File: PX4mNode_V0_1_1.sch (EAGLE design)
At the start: 140 parts, among them J201 DF13C-6P-1.25V, J202 DF13C-6P-1.25V, J203 DF13C-6P-1.25V, J301 DF13C-4P-1.25V, J401 DF13C-7P-1.25V, J402 DF13-4P-1.25V, J403 DF13C-4P-1.25V, J404 DF13C-4P-1.25V, J405 DF13C-4P-1.25V, J801 DF13C-3P-1.25V, M3_MOUNT1101 MOUNT-HOLE3.1MM, M3_MOUNT1102 MOUNT-HOLE3.1MM, M3_MOUNT1103 MOUNT-HOLE3.1MM, M3_MOUNT1104 MOUNT-HOLE3.1MM, U101 STM32F4X7VX, U401 MAX3051, U402 MAX3051, X101 3.2x2.5 mm / 24 MHz / 15 ppm

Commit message: Renumber
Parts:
- renumbered JP1 to JP1001, JP2 to JP1002, JP3 to JP702, R1 to R1001, R2 to R1002
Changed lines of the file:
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@@
 <attribute name="PARTNO" value="MSS1P4-M3/89A"/>
 </part>
-<part name="JP1" library="SparkFun-Connectors" deviceset="M01" device="SMD-4.5X1.5"/>
-<part name="JP2" library="SparkFun-Connectors" deviceset="M01" device="SMD-4.5X1.5"/>
-<part name="R1" library="pixhawk2" deviceset="RESISTOR" device="0402-RES" value="220R">
+<part name="JP1001" library="SparkFun-Connectors" deviceset="M01" device="SMD-4.5X1.5"/>
+<part name="JP1002" library="SparkFun-Connectors" deviceset="M01" device="SMD-4.5X1.5"/>
+<part name="R1001" library="pixhawk2" deviceset="RESISTOR" device="0402-RES" value="220R">
 <attribute name="PARTNO" value="RC0402FR-07220RL"/>
 </part>
-<part name="R2" library="pixhawk2" deviceset="RESISTOR" device="0402-RES" value="220R">
+<part name="R1002" library="pixhawk2" deviceset="RESISTOR" device="0402-RES" value="220R">
 <attribute name="PARTNO" value="RC0402FR-07220RL"/>
 </part>
-<part name="JP3" library="SparkFun-Connectors" deviceset="M01" device="SMD-4.5X1.5"/>
+<part name="JP702" library="SparkFun-Connectors" deviceset="M01" device="SMD-4.5X1.5"/>
 </parts>
 <sheets>
@@
 <attribute name="PARTNO" x="205.74" y="127" size="1.778" layer="96" rot="MR90" display="off"/>
 </instance>
-<instance part="JP3" gate="G$1" x="195.58" y="91.44"/>
+<instance part="JP702" gate="G$1" x="195.58" y="91.44"/>
 </instances>
 <busses>
@@
 <wire x1="233.68" y1="91.44" x2="233.68" y2="96.52" width="0.1524" layer="91"/>
 <junction x="223.52" y="91.44"/>
-<pinref part="JP3" gate="G$1" pin="1"/>
+<pinref part="JP702" gate="G$1" pin="1"/>
 <wire x1="203.2" y1="91.44" x2="223.52" y2="91.44" width="0.1524" layer="91"/>
 </segment>
@@
 <instance part="J1001" gate="-CH7" x="101.6" y="129.54"/>
 <instance part="J1001" gate="-CH8" x="101.6" y="134.62"/>
-<instance part="JP1" gate="G$1" x="106.68" y="71.12" rot="R180"/>
-<instance part="JP2" gate="G$1" x="106.68" y="53.34" rot="R180"/>
-<instance part="R1" gate="G$1" x="71.12" y="71.12" rot="R180">
+<instance part="JP1001" gate="G$1" x="106.68" y="71.12" rot="R180"/>
+<instance part="JP1002" gate="G$1" x="106.68" y="53.34" rot="R180"/>
+<instance part="R1001" gate="G$1" x="71.12" y="71.12" rot="R180">
 <attribute name="PARTNO" x="71.12" y="71.12" size="1.778" layer="96" rot="R90" display="off"/>
 </instance>
-<instance part="R2" gate="G$1" x="71.12" y="53.34" rot="R180">
+<instance part="R1002" gate="G$1" x="71.12" y="53.34" rot="R180">
 <attribute name="PARTNO" x="71.12" y="53.34" size="1.778" layer="96" rot="R90" display="off"/>
 </instance>
@@
 <net name="N$19" class="0">
 <segment>
-<pinref part="JP1" gate="G$1" pin="1"/>
-<pinref part="R1" gate="G$1" pin="1"/>
+<pinref part="JP1001" gate="G$1" pin="1"/>
+<pinref part="R1001" gate="G$1" pin="1"/>
 <wire x1="99.06" y1="71.12" x2="76.2" y2="71.12" width="0.1524" layer="91"/>
 </segment>
@@
 <net name="N$23" class="0">
 <segment>
-<pinref part="JP2" gate="G$1" pin="1"/>
-<pinref part="R2" gate="G$1" pin="1"/>
+<pinref part="JP1002" gate="G$1" pin="1"/>
+<pinref part="R1002" gate="G$1" pin="1"/>
 <wire x1="99.06" y1="53.34" x2="76.2" y2="53.34" width="0.1524" layer="91"/>
 </segment>
@@
 <wire x1="40.64" y1="71.12" x2="66.04" y2="71.12" width="0.1524" layer="91"/>
 <label x="40.64" y="71.12" size="1.27" layer="95" rot="R180" xref="yes"/>
-<pinref part="R1" gate="G$1" pin="2"/>
+<pinref part="R1001" gate="G$1" pin="2"/>
 </segment>
 </net>
@@
 <label x="40.64" y="53.34" size="1.27" layer="95" rot="R180" xref="yes"/>
 <wire x1="40.64" y1="53.34" x2="66.04" y2="53.34" width="0.1524" layer="91"/>
-<pinref part="R2" gate="G$1" pin="2"/>
+<pinref part="R1002" gate="G$1" pin="2"/>
 </segment>
 </net>

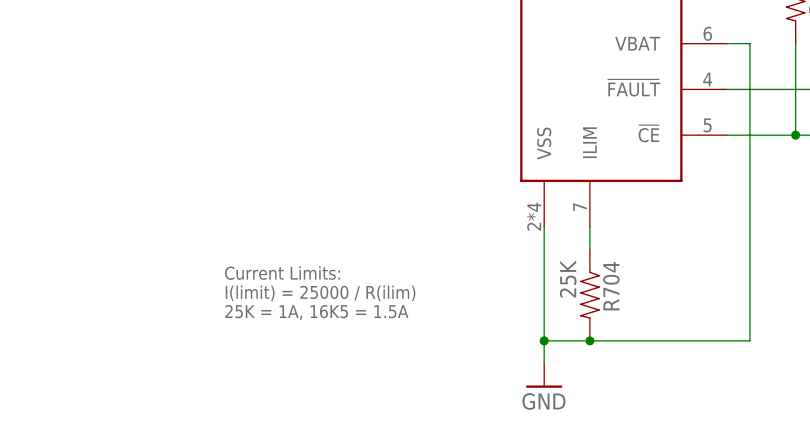
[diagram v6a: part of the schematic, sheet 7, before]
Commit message: BOM EXLUDES added to solder jumpers, 0.1" conns etc..
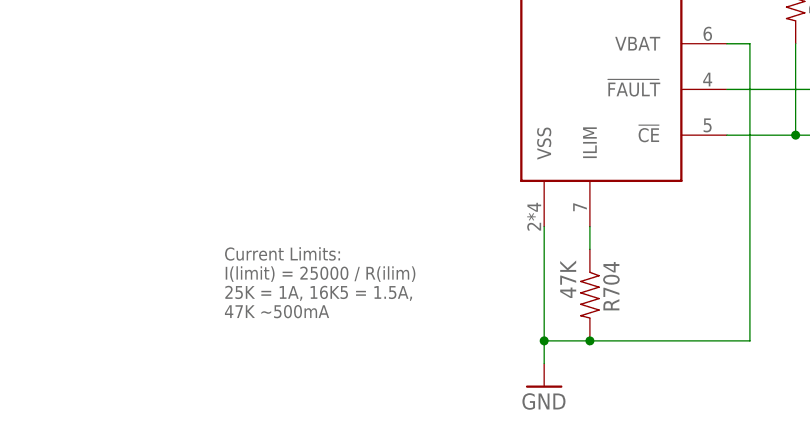
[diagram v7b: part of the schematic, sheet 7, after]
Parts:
- D901, J$401, J1001, JP1001, JP1002, JP201, JP202, JP701, JP702, JP901, SJ401, SJ402, SJ403: BOM (none) -> EXCLUDE
- R704: value 25K -> 47K; PARTNO RMCF0402FT25K5 -> RMCF0402FT47K
- U$202: PARTNO (none) -> 74LVC2GU04
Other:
- note added: "Current Limits: I(limit) = 25000 / R(ilim) 25K = 1A, 16K5 = 1.5A, 47K ~500mA"
- note added: "DO NOT FIT"
- note removed: "Current Limits: I(limit) = 25000 / R(ilim) 25K = 1A, 16K5 = 1.5A"

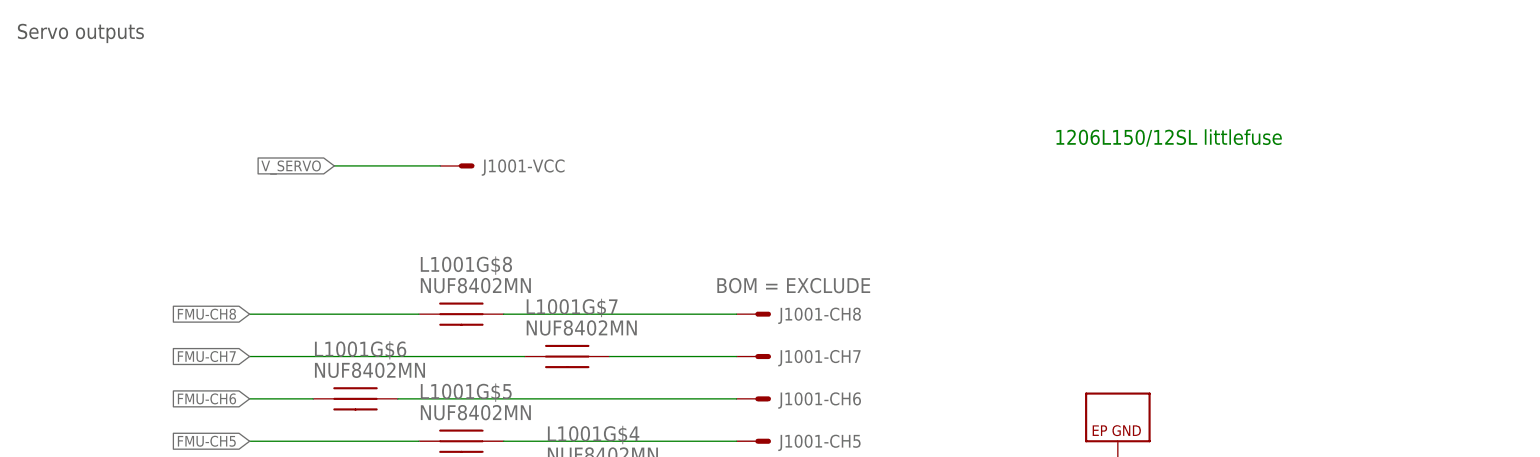
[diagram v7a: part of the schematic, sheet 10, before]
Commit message: a few bom tweaks
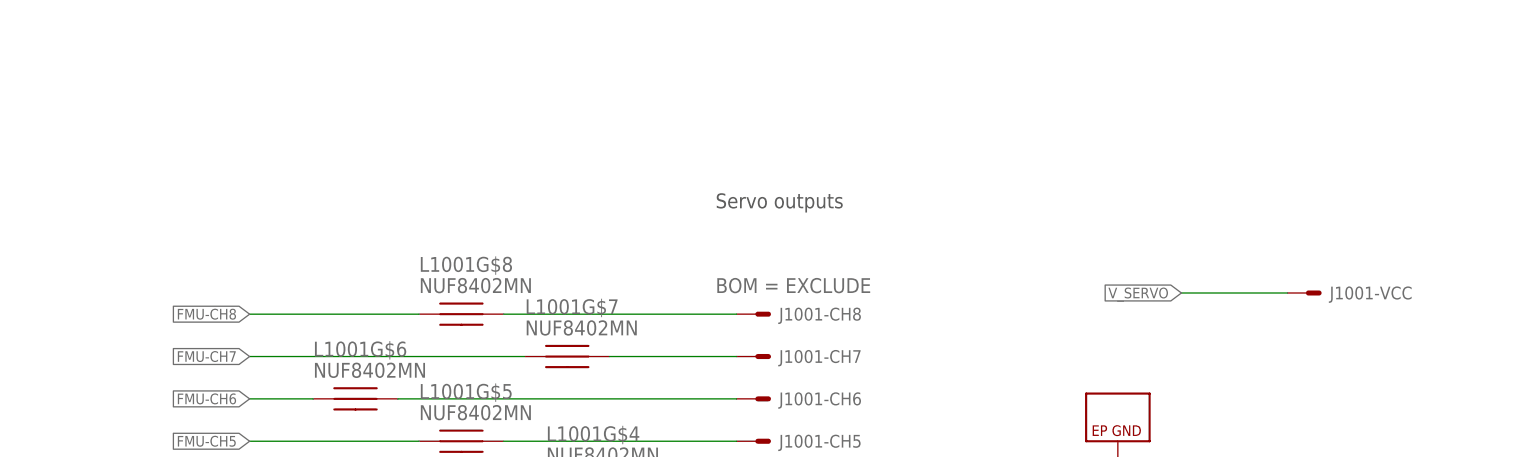
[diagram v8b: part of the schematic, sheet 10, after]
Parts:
- D902, D903: PARTNO (none) -> B340A
- J301, J403, J404, J405: device con-hirose-df13:DF13-4P-1.25V -> PX4FMUlite_V0_1:DF13-4P-1.25V
- J402: value DF13-4P-1.25V -> DF13C-4P-1.25V; device con-hirose-df13:DF13-4P-1.25V -> PX4FMUlite_V0_1:DF13-4P-1.25V
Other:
- note added: "FMU Power FMU Reset Battery backup Peripheral power control"
- note added: "FMU Serial ports SBUS interface Spektrum interface"
- note added: "FMU SoC Ports"
- note added: "LEDs Safety switch"
- note added: "Power regulation"
- note added: "SPI Dual I2C Dual CAN Aux ADC ports"
- note added: "USB Flash SWD Debug connector"
- note removed: "1206L150/12SL littlefuse"
- note removed: "FMU Power and Reset"
- note removed: "FMU Serial ports"
- note removed: "FMU SoC Ports FRAM"
- note removed: "LEDs Piezo driver Safety switch"
- note removed: "Power source selector"
- note removed: "SPI I2C Analog pressure CAN Aux ADC ports"
- note removed: "USB Flash Expansion"
- moved on the sheet: J1001-VCC
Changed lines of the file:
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@@
 <attribute name="PARTNO" value="*"/>
 </part>
-<part name="J301" library="con-hirose-df13" deviceset="DF13-4P-1.25" device="V" value="DF13C-4P-1.25V">
+<part name="J301" library="PX4FMUlite_V0_1" deviceset="DF13-4P-1.25" device="V" value="DF13C-4P-1.25V">
 <attribute name="PARTNO" value="DF13C-4P-1.25V(20)"/>
 </part>
@@
 </part>
 <part name="GND31" library="pixhawk2" deviceset="GND" device=""/>
-<part name="J403" library="con-hirose-df13" deviceset="DF13-4P-1.25" device="V" value="DF13C-4P-1.25V">
+<part name="J403" library="PX4FMUlite_V0_1" deviceset="DF13-4P-1.25" device="V" value="DF13C-4P-1.25V">
 <attribute name="PARTNO" value="DF13C-4P-1.25V(20)"/>
 </part>
@@
 <attribute name="PARTNO" value="MAX3051EKA"/>
 </part>
-<part name="J405" library="con-hirose-df13" deviceset="DF13-4P-1.25" device="V" value="DF13C-4P-1.25V">
+<part name="J405" library="PX4FMUlite_V0_1" deviceset="DF13-4P-1.25" device="V" value="DF13C-4P-1.25V">
 <attribute name="PARTNO" value="DF13C-4P-1.25V(20)"/>
 </part>
@@
 </part>
 <part name="GND15" library="pixhawk2" deviceset="GND" device=""/>
-<part name="J402" library="con-hirose-df13" deviceset="DF13-4P-1.25" device="V" value="DF13-4P-1.25V">
+<part name="J402" library="PX4FMUlite_V0_1" deviceset="DF13-4P-1.25" device="V" value="DF13C-4P-1.25V">
 <attribute name="PARTNO" value="DF13C-4P-1.25V(20)"/>
 </part>
@@
 <attribute name="PARTNO" value="MAX3051EKA"/>
 </part>
-<part name="J404" library="con-hirose-df13" deviceset="DF13-4P-1.25" device="V" value="DF13C-4P-1.25V">
+<part name="J404" library="PX4FMUlite_V0_1" deviceset="DF13-4P-1.25" device="V" value="DF13C-4P-1.25V">
 <attribute name="PARTNO" value="DF13C-4P-1.25V(20)"/>
 </part>
@@
 <attribute name="BOM" value="EXCLUDE"/>
 </part>
-<part name="D902" library="SparkFun-DiscreteSemi" deviceset="DIODE" device="SMA" value="B340A"/>
-<part name="D903" library="SparkFun-DiscreteSemi" deviceset="DIODE" device="SMA" value="B340A"/>
+<part name="D902" library="SparkFun-DiscreteSemi" deviceset="DIODE" device="SMA" value="B340A">
+<attribute name="PARTNO" value="B340A"/>
+</part>
+<part name="D903" library="SparkFun-DiscreteSemi" deviceset="DIODE" device="SMA" value="B340A">
+<attribute name="PARTNO" value="B340A"/>
+</part>
 <part name="U$601" library="PX4lite" deviceset="TPS6303X" device=""/>
 <part name="L$601" library="ti_tps_soln2" deviceset="XFL4020-222MEB" device=""/>
@@
 <plain>
 <text x="162.56" y="15.24" size="2.1844" layer="94" font="vector" ratio="10">FMU SoC Ports
-FRAM</text>
+</text>
 <text x="7.62" y="5.08" size="1.27" layer="91">Note: MAG/ACCEL/GYRO_DRDY pins chosen
 for both timer capture and separate
@@
 <sheet>
 <plain>
-<text x="165.1" y="17.78" size="2.1844" layer="94">FMU Serial ports</text>
+<text x="165.1" y="17.78" size="2.1844" layer="94">FMU Serial ports
+SBUS interface
+Spektrum interface</text>
 <text x="233.68" y="121.92" size="1.778" layer="97">SERIAL2</text>
 <text x="233.68" y="154.94" size="1.778" layer="97">SERIAL1</text>
@@
 <text x="162.56" y="12.7" size="2.1844" layer="94">USB
 Flash
-Expansion</text>
+SWD Debug connector</text>
 <text x="93.98" y="111.76" size="1.4224" layer="97">To be used with panel-
 mount micro USB connectors:
@@
 <text x="228.6" y="170.18" size="1.778" layer="97">AUX ADC PORTS</text>
 <text x="165.1" y="7.62" size="1.778" layer="94">SPI
-I2C
-Analog pressure
-CAN
+Dual I2C
+Dual CAN
 Aux ADC ports</text>
 <text x="22.86" y="170.18" size="1.778" layer="91">Note: SPI port is UNBUFFERED; only suitable for short connections.</text>
@@
 <sheet>
 <plain>
-<text x="165.1" y="17.78" size="2.1844" layer="94">Power source selector</text>
+<text x="165.1" y="17.78" size="2.1844" layer="94">Power regulation</text>
 </plain>
 <instances>
@@
 <sheet>
 <plain>
-<text x="165.1" y="17.78" size="1.9304" layer="94" font="vector" ratio="10">FMU Power and Reset</text>
+<text x="165.1" y="7.62" size="1.9304" layer="94" font="vector" ratio="10">FMU Power
+FMU Reset
+Battery backup
+Peripheral power control</text>
 <text x="187.96" y="170.18" size="1.27" layer="97" font="vector">Bypass caps as close to device pins as possible.</text>
 <text x="71.12" y="160.02" size="1.27" layer="97">Note: Maximise copper area connected
@@
 <plain>
 <text x="165.1" y="10.16" size="2.1844" layer="94">LEDs
-Piezo driver
 Safety switch</text>
 <text x="78.74" y="78.74" size="1.778" layer="97">Switch: E-Switch LP1OA1AR</text>
@@
 <attribute name="BOM" x="81.28" y="86.36" size="1.778" layer="96" rot="R90" display="off"/>
 </instance>
-<instance part="D902" gate="G$1" x="104.14" y="127"/>
-<instance part="D903" gate="G$1" x="116.84" y="139.7" rot="R270"/>
+<instance part="D902" gate="G$1" x="104.14" y="127">
+<attribute name="PARTNO" x="104.14" y="127" size="1.778" layer="96" display="off"/>
+</instance>
+<instance part="D903" gate="G$1" x="116.84" y="139.7" rot="R270">
+<attribute name="PARTNO" x="116.84" y="139.7" size="1.778" layer="96" rot="R270" display="off"/>
+</instance>
 <instance part="JP901" gate="G$1" x="66.04" y="154.94">
 <attribute name="BOM" x="66.04" y="154.94" size="1.778" layer="96" display="off"/>
@@
 <text x="165.1" y="15.24" size="2.1844" layer="94">Servo Header
 S.Bus interface</text>
-<text x="12.7" y="167.64" size="1.778" layer="97">Servo outputs</text>
-<text x="137.16" y="154.94" size="1.778" layer="91">1206L150/12SL littlefuse</text>
+<text x="96.52" y="147.32" size="1.778" layer="97">Servo outputs</text>
 </plain>
 <instances>
@@
 <instance part="L1001" gate="G$9" x="144.78" y="116.84"/>
 <instance part="J1001" gate="-GND" x="154.94" y="111.76"/>
-<instance part="J1001" gate="-VCC" x="66.04" y="152.4"/>
+<instance part="J1001" gate="-VCC" x="167.64" y="137.16"/>
 <instance part="J1001" gate="-CH1" x="101.6" y="99.06"/>
 <instance part="J1001" gate="-CH2" x="101.6" y="104.14"/>
@@
 <net name="V_SERVO" class="1">
 <segment>
-<label x="50.8" y="152.4" size="1.27" layer="95" rot="R180" xref="yes"/>
+<label x="152.4" y="137.16" size="1.27" layer="95" rot="R180" xref="yes"/>
 <pinref part="J1001" gate="-VCC" pin="S"/>
-<wire x1="63.5" y1="152.4" x2="50.8" y2="152.4" width="0.1524" layer="91"/>
+<wire x1="165.1" y1="137.16" x2="152.4" y2="137.16" width="0.1524" layer="91"/>
 </segment>
 </net>
